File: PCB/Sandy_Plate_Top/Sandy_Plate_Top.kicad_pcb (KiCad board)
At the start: 2 copper layers, 285 x 37 mm, 21 parts

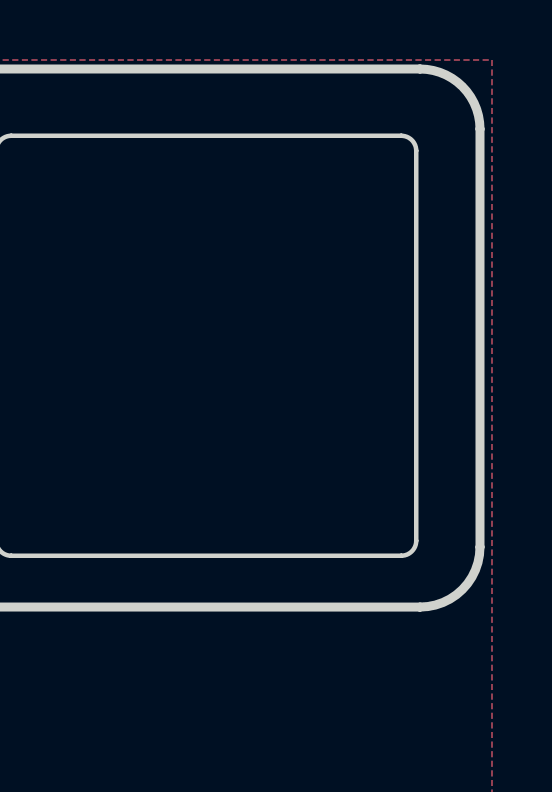
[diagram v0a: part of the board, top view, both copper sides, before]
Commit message: 製作したリビジョンを知りたいので、バージョン表記からリビジョン番号による表記へ変更
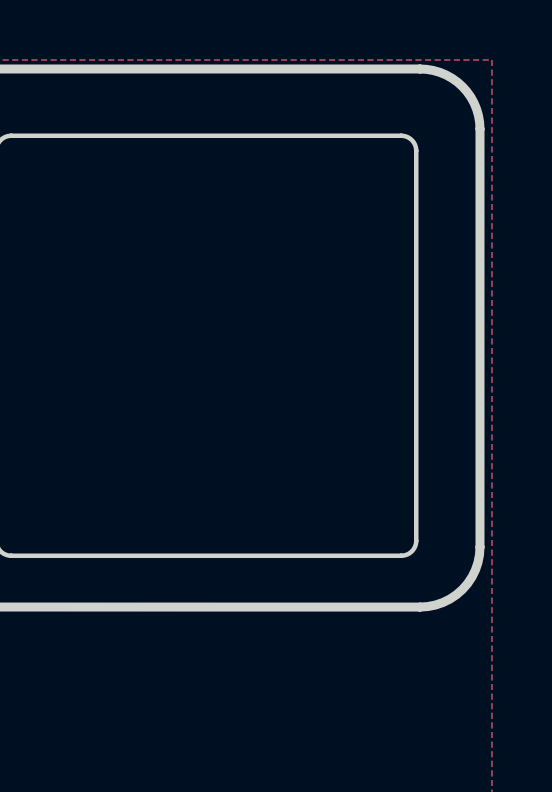
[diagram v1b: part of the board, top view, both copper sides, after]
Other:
- board text added: "#Sandy_kbd DN0020, Plate for Top by @jpskenn"
- board text removed: "#Sandy_kbd v.0.2, Plate for Top by @jpskenn"
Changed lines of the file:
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@@
     (fp_arc (start 140.35 -3.025) (mid 140.203553 -2.671447) (end 139.85 -2.525)
       (stroke (width 0.15) (type solid)) (layer "Edge.Cuts"))
-    (fp_arc (start 140.475 -18.75004) (mid 141.889257 -18.164285) (end 142.475 -16.75004)
+    (fp_arc (start 140.475 -18.75004) (mid 141.889222 -18.164279) (end 142.475 -16.75004)
       (stroke (width 0.3) (type solid)) (layer "Edge.Cuts"))
-    (fp_arc (start 142.475 -2.814254) (mid 141.889203 -1.400035) (end 140.475 -0.814254)
+    (fp_arc (start 142.475 -2.814254) (mid 141.889197 -1.40007) (end 140.475 -0.814254)
       (stroke (width 0.3) (type solid)) (layer "Edge.Cuts"))
     (group "" (id b45a4e6d-43e9-43f3-99a8-109a97b956a9)
@@
     (effects (font (size 1.5 1.5) (thickness 0.3)) (justify mirror))
   )
-  (gr_text "#Sandy_kbd v.0.2, Plate for Top by @jpskenn" (at 193.69906 36.528405) (layer "B.SilkS")
+  (gr_text "#Sandy_kbd DN0020, Plate for Top by @jpskenn" (at 193.69906 36.528405) (layer "B.SilkS")
     (effects (font (size 1.6 1.6) (thickness 0.2)) (justify left mirror))
   )

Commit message: 修正：強度確保のため、Topプレートの枠を太くした
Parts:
- REF**: footprint locallib:60_Outline-Sandy-Plate-Top -> locallib:60_Outline-Sandy-Plate-Top2-thick-frame
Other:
- board size 285 x 37 mm -> 285 x 37.6 mm
- board text added: "Back Side"

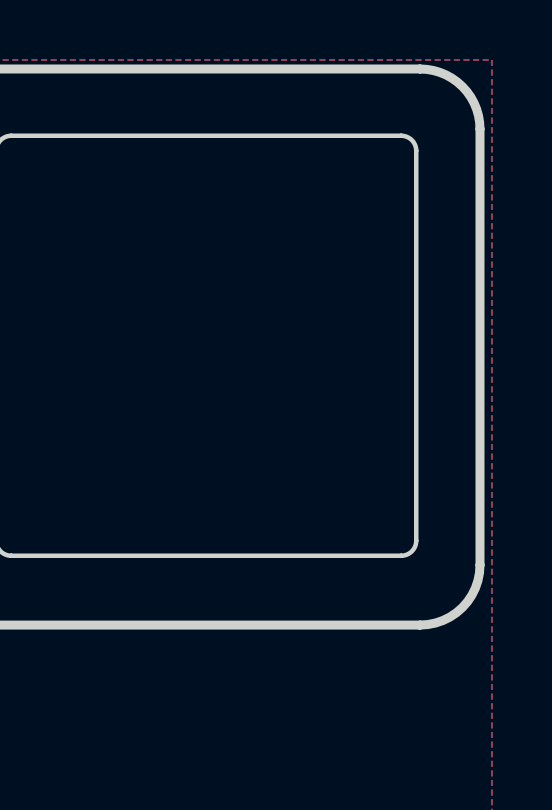
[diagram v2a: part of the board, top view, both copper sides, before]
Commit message: 改善：基板うら側を示すシルクを目立つように変更
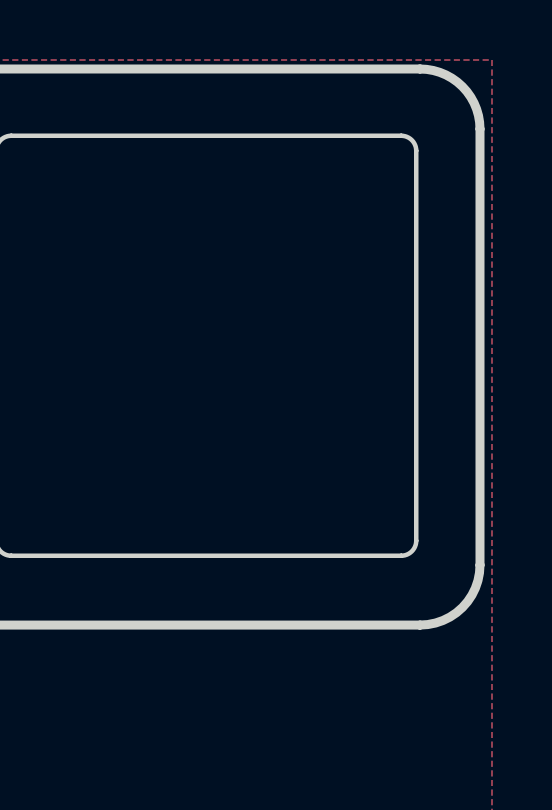
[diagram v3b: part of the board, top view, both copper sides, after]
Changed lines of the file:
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@@
     (fp_arc (start 35.575 16.025) (mid 35.428553 16.378553) (end 35.075 16.525)
       (stroke (width 0.15) (type solid)) (layer "Edge.Cuts"))
-    (fp_arc (start 37.375 1.221492) (mid 37.795526 0.206288) (end 38.810746 -0.214254)
+    (fp_arc (start 37.375 1.221492) (mid 37.795535 0.206282) (end 38.810746 -0.214254)
       (stroke (width 0.3) (type solid)) (layer "Edge.Cuts"))
     (fp_arc (start 37.375 16.84996) (mid 36.789208 18.264168) (end 35.375 18.84996)
@@
     (fp_arc (start 140.35 -3.025) (mid 140.203553 -2.671447) (end 139.85 -2.525)
       (stroke (width 0.15) (type solid)) (layer "Edge.Cuts"))
-    (fp_arc (start 140.475 -18.75004) (mid 141.889257 -18.164285) (end 142.475 -16.75004)
+    (fp_arc (start 140.475 -18.75004) (mid 141.889222 -18.164279) (end 142.475 -16.75004)
       (stroke (width 0.3) (type solid)) (layer "Edge.Cuts"))
-    (fp_arc (start 142.475 -2.214254) (mid 141.889197 -0.80007) (end 140.475 -0.214254)
+    (fp_arc (start 142.475 -2.214254) (mid 141.889203 -0.800035) (end 140.475 -0.214254)
       (stroke (width 0.3) (type solid)) (layer "Edge.Cuts"))
     (group "" (id 33ddfa32-f34b-4d4f-9ba0-86da081a4319)
@@
   )
   (gr_text "Back Side" (at 281.80531 27.003405 90) (layer "B.SilkS" knockout)
-    (effects (font (size 1.8 1.8) (thickness 0.24)) (justify mirror))
+    (effects (font (size 1.8 1.8) (thickness 0.28) italic) (justify mirror))
   )
   (gr_text "JLCJLCJLCJLC" (at 34.15531 27.003405 90) (layer "B.SilkS")
